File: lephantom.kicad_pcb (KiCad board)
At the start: 2 copper layers, 113.4 x 83.6 mm, 19 parts, among them J1 MJ-4PP-9, SW10 SW_PUSH, SW11 SW_PUSH, SW12 SW_PUSH, SW15 SW_PUSH, SW16 SW_PUSH, SW17 SW_PUSH, SW2 SW_PUSH, SW20 SW_PUSH, SW21 SW_PUSH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

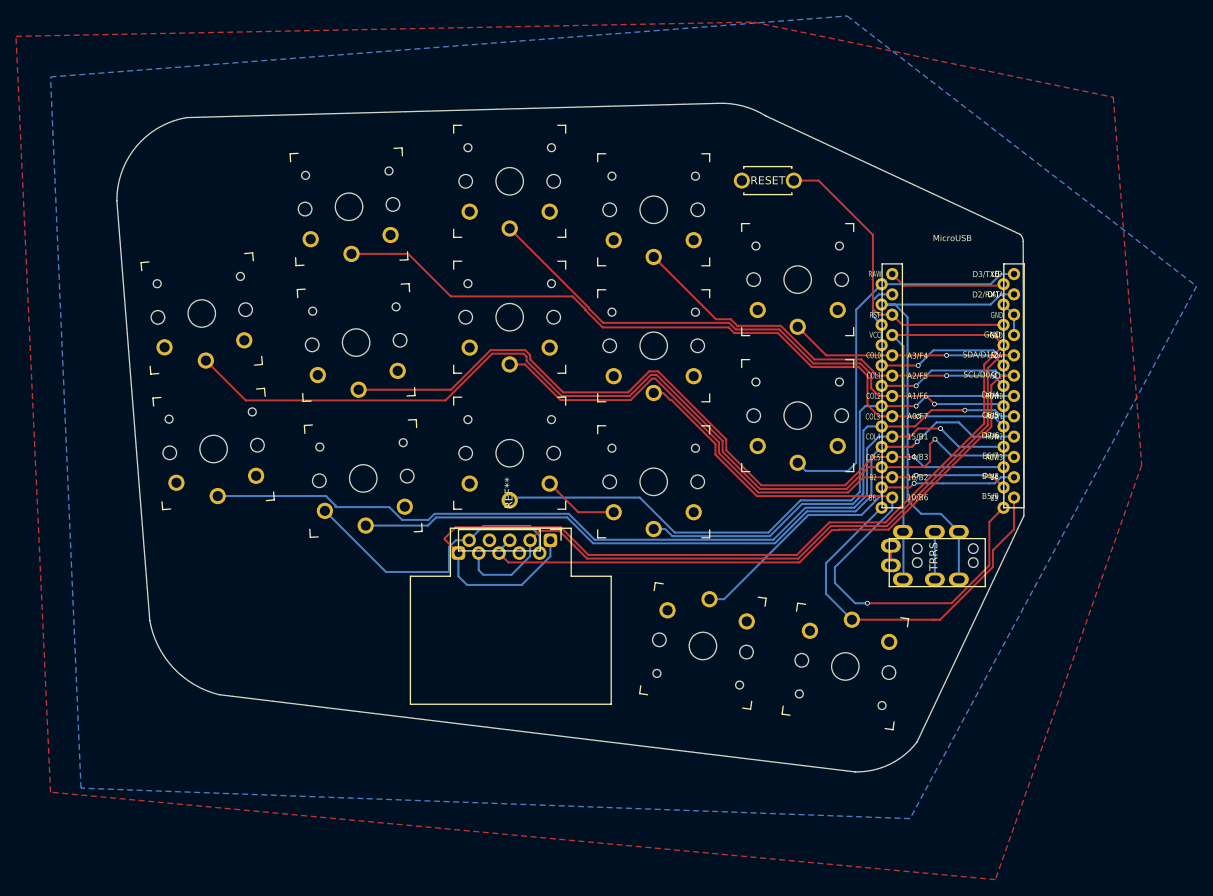
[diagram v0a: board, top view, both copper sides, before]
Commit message: Reduce fill zone padding
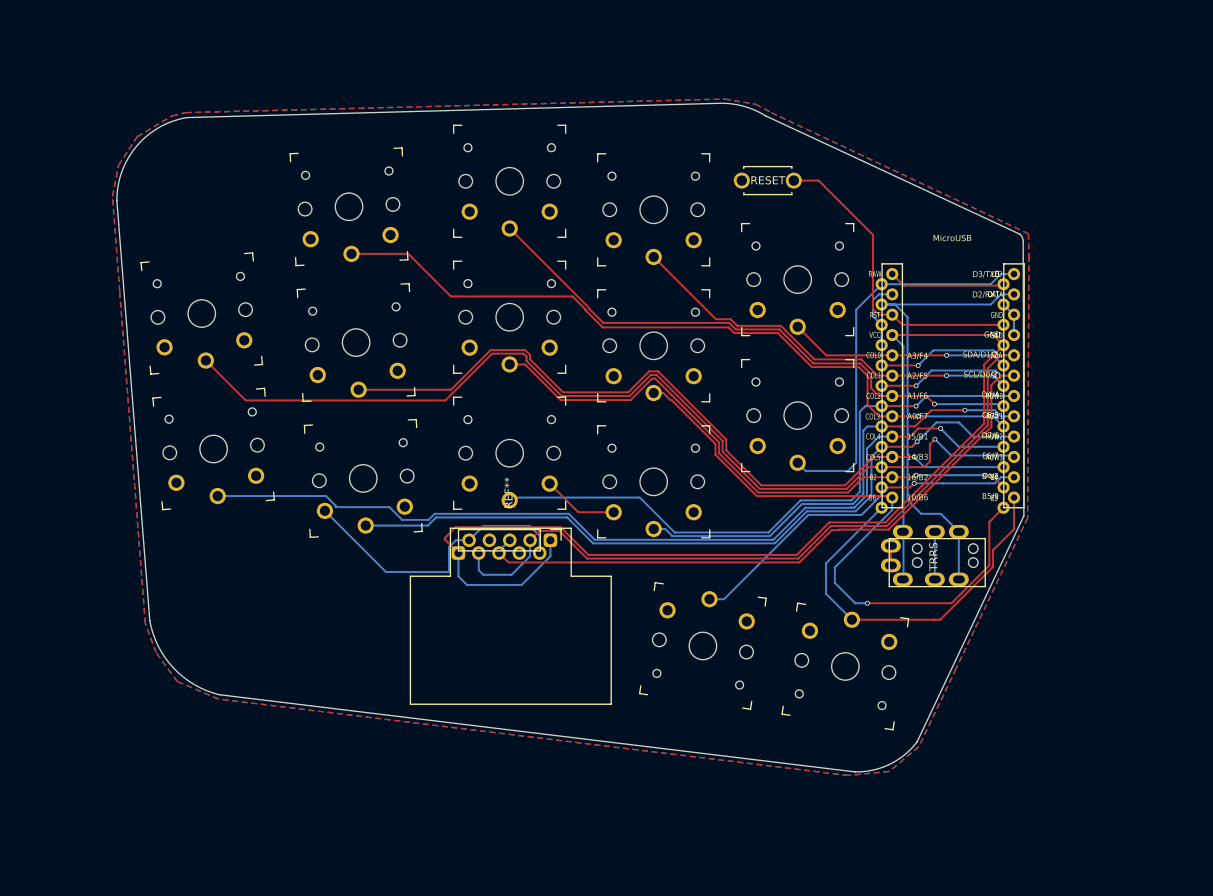
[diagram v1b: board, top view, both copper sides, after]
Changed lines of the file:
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@@
   (segment (start 141.549001 38.028999) (end 141.732 37.846) (width 0.25) (layer "F.Cu") (net 23))
   (segment (start 129.271399 38.028999) (end 141.549001 38.028999) (width 0.25) (layer "F.Cu") (net 23))
-  (zone (net 6) (net_name "GND") (layer "F.Cu") (hatch edge 0.508)
+  (zone (net 6) (net_name "GND") (layers F&B.Cu) (hatch edge 0.508)
     (connect_pads (clearance 0.508))
-    (min_thickness 0.254)
-    (fill yes (thermal_gap 0.508) (thermal_bridge_width 0.508))
+    (min_thickness 0.254) (filled_areas_thickness no)
+    (fill yes (thermal_gap 0.508) (thermal_bridge_width 0.508) (island_removal_mode 1) (island_area_min 0))
     (polygon
       (pts
-        (xy 155.448 14.478)
-        (xy 159.004 60.452)
-        (xy 140.716 112.268)
-        (xy 22.606 101.346)
-        (xy 18.288 6.858)
-        (xy 110.49 5.08)
+        (xy 110.75 15.35)
+        (xy 112.7 16.4)
+        (xy 144.85 31.55)
+        (xy 144.9 34.3)
+        (xy 144.75 67.05)
+        (xy 135.8 85.9)
+        (xy 131.15 95.65)
+        (xy 127.45 98.75)
+        (xy 122.3 99.25)
+        (xy 43.6 89.7)
+        (xy 38.45 87.5)
+        (xy 35.8 83.9)
+        (xy 34.45 80.25)
+        (xy 31.25 38.75)
+        (xy 30.35 26.85)
+        (xy 31.1 23)
+        (xy 33.45 19.4)
+        (xy 37.8 16.8)
+        (xy 39.5 16.4)
+        (xy 106.85 14.7)
       )
     )
-  )
-  (zone (net 6) (net_name "GND") (layer "B.Cu") (hatch edge 0.508)
-    (connect_pads (clearance 0.508))
-    (min_thickness 0.254)
-    (fill yes (thermal_gap 0.508) (thermal_bridge_width 0.508))
-    (polygon
-      (pts
-        (xy 165.862 38.1)
-        (xy 130.048 104.648)
-        (xy 26.416 100.838)
-        (xy 22.606 11.938)
-        (xy 122.174 4.318)
-      )
-    )
